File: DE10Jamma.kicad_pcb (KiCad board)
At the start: 2 copper layers, 114.6 x 83.4 mm, 104 parts, among them J1 Arduino 3-7, J10 5V TO DE10, J2 Arduino 8-SCL, J3 FAN 12V, J4 FAN 5V, J5 FAN 3V3, J6 Arduino Reset, J7 GPIO1, J8 Jamma_con, J9 CPS1 KICK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

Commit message: clean before sending to manufacture
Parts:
- added J11: 0.1" kick, Connector_PinHeader_2.54mm:PinHeader_1x10_P2.54mm_Vertical, F.Cu at (93.7, 85.5)
- moved R8 17.2 mm to (186.4, 98.0)
- moved R73 2.99 mm to (103.3, 47.9)
- moved R113 1.74 mm to (160.4, 66.8)
- moved C38 1.17 mm to (104.9, 52.7)
- moved C11 0.26 mm to (189.1, 85.7)
- moved R110 0.13 mm to (159.2, 59.2)
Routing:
- net GND: track 331.9 -> 86.3 mm, vias 81 -> 121
- net Net-(C7-Pad1): track 68.6 -> 39.2 mm
- net /P1_BUTTON5: track 81.9 -> 97.4 mm
- net /P1_BUTTON4: track 110.2 -> 125.4 mm
- net Net-(R8-Pad1): track 7.62 -> 20.4 mm
- net /JAMMA_P2_BUTTON4: track 76.5 -> 84.6 mm
- net /JAMMA_SPEAKER_L: track 85.1 -> 77.5 mm
- net +12V: track 94.5 -> 89.0 mm, vias 1 -> 2
- net /JAMMA_P2_BUTTON6: track 4.00 -> 9.02 mm
- net /JAMMA_P2_BUTTON5: track 4.00 -> 9.00 mm
- net /JAMMA_P1_BUTTON6: track 4.00 -> 8.95 mm
- net /JAMMA_P1_BUTTON5: track 4.00 -> 8.94 mm
- net /JAMMA_P1_BUTTON4: track 55.8 -> 60.5 mm
- net +5V: track 104.9 -> 109.3 mm, vias 2 -> 4
- net +5VL: track 113.1 -> 117.3 mm
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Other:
- board text added: "12V"
- board text added: "3V3"
- board text added: "5V"
- board text added: "BLUE"
- board text added: "CPS1 KICK"
- board text added: "DE10 Jamma v1.0"
- board text added: "GND"
- board text added: "GREEN"
- board text added: "L"
- board text added: "P1B4"
- board text added: "P1B5"
- board text added: "P1B6"
- board text added: "P2B4"
- board text added: "P2B5"
- board text added: "P2B6"
- board text added: "R"
- board text added: "RED"
- board text added: "VOLUME"
- board text added: "https://github.com/MisterJamma/DE10Jamma"
- board text removed: "DE10 Jamma"

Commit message: Add mono/stereo jumper. Remove out of date pdf
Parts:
- added JP1: Mono/Stereo, Connector_PinHeader_2.54mm:PinHeader_1x03_P2.54mm_Vertical, F.Cu at (186.9, 60.7)
- added R5: 10k, Capacitor_SMD:C_0805_2012Metric, B.Cu at (192.7, 67.0)
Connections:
- U1 pad 1: Net-(C5-Pad2) -> Net-(JP1-Pad1)
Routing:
- net Net-(JP1-Pad1): track 0.00 -> 10.8 mm
- net Net-(C6-Pad2): track 2.29 -> 12.1 mm
- net Net-(C5-Pad2): track 2.29 -> 7.28 mm
- net GND: vias 121 -> 120
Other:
- board text added: "JLCJLCJLCJLC"
- board text added: "MONO/STEREO"

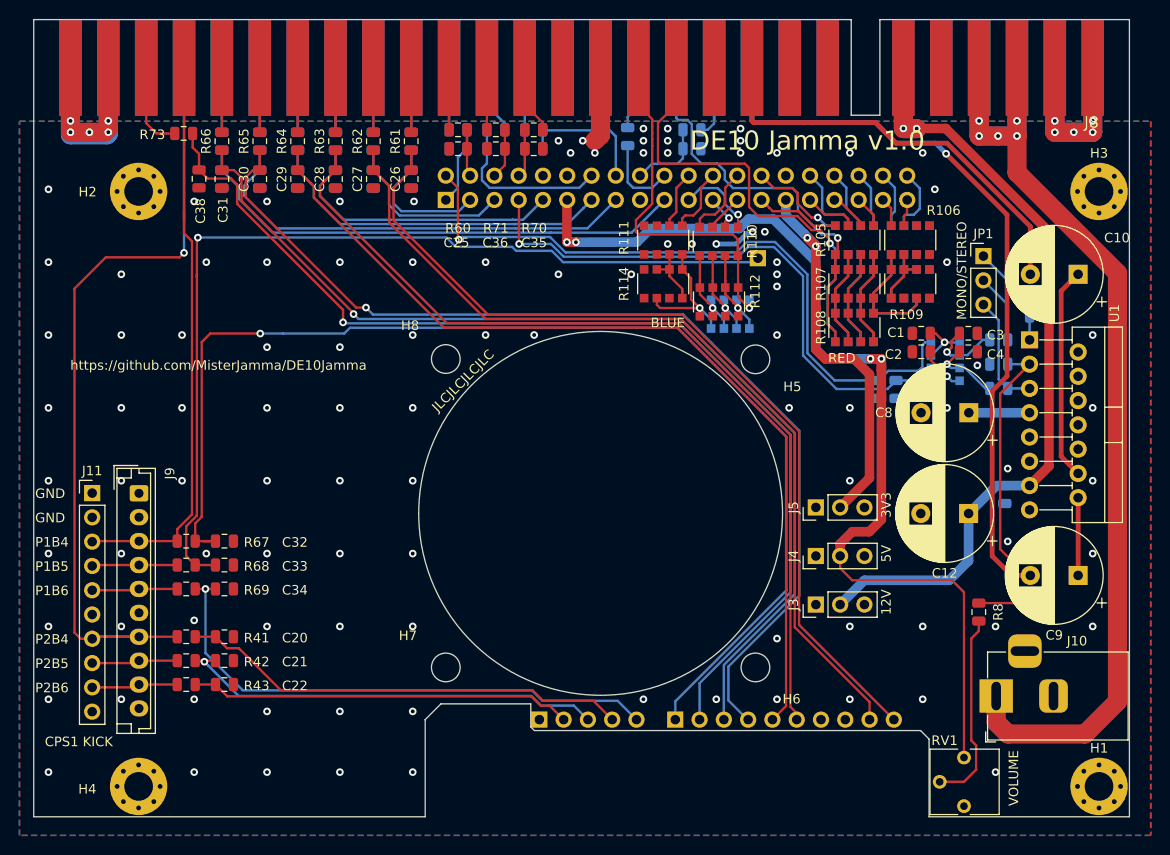
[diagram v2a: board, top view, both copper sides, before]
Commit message: Use smaller footprint for r-packs. Rework mono/stereo jumper to avoid potential DC path issues if inputs have DC offset. General routing & silk screen cleanup.
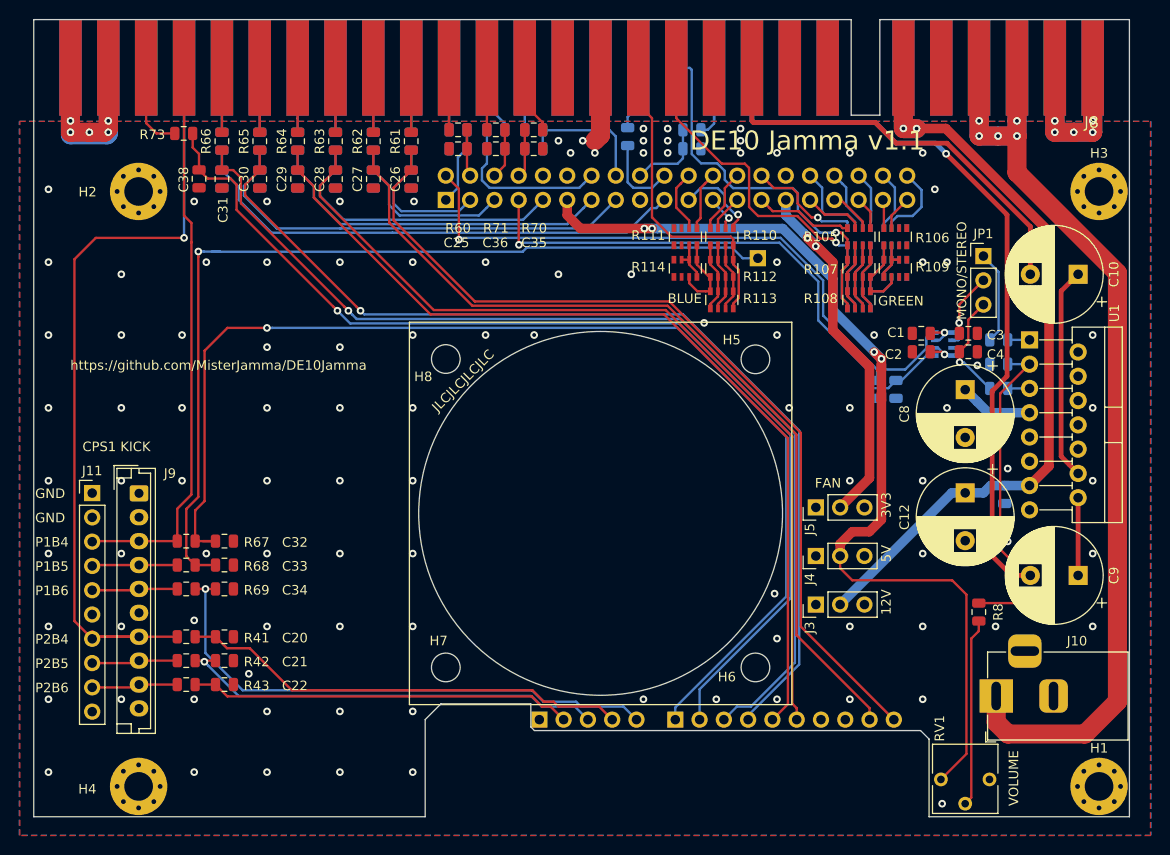
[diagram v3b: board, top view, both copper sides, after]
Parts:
- removed R5: 10k, Capacitor_SMD:C_0805_2012Metric
- R100, R101, R102, R103, R104, R105, R106, R107, R108, R109, R110, R111, R112, R114, R4: footprint Resistor_SMD:R_Array_Convex_4x1206 -> Resistor_SMD:R_Array_Convex_4x0603
- R113: footprint Resistor_SMD:R_Array_Convex_4x1206 -> Resistor_SMD:R_Array_Convex_4x0603; moved to F.Cu
- moved R112 3.52 mm to (159.6, 62.0)
- moved RV1 3.32 mm to (182.5, 115.5), turned to 270 degrees
- moved R103 2.92 mm to (173.9, 65.3)
- moved R108 2.92 mm to (173.9, 65.3)
- moved R114 2.83 mm to (155.7, 62.0)
- moved C8 2.44 mm to (185.0, 74.7), turned to 270 degrees
- moved R111 2.35 mm to (155.7, 58.7)
- moved R104 2.25 mm to (177.7, 62.0)
- moved R109 2.25 mm to (177.7, 62.0)
- moved C12 2.19 mm to (185.0, 85.5), turned to 270 degrees
- moved R4 1.85 mm to (182.7, 69.9)
- moved R113 1.73 mm to (159.6, 65.3), turned to 270 degrees
- moved R102 1.68 mm to (173.9, 62.0)
- moved R107 1.68 mm to (173.9, 62.0)
- moved R101 1.60 mm to (177.7, 58.7)
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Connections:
- C5 pad 1: Net-(C3-Pad1) -> Net-(C5-Pad1)
- H5 pad 1: (no net) -> GND
- H6 pad 1: (no net) -> GND
- H7 pad 1: (no net) -> GND
- H8 pad 1: (no net) -> GND
- J1 pad 1: Net-(J1-Pad1) -> (no net)
- J11 pad 10: Net-(J11-Pad10) -> (no net)
- J11 pad 6: Net-(J11-Pad6) -> (no net)
- J2 pad 8: Net-(J2-Pad8) -> (no net)
- J3 pad 3: Net-(J3-Pad3) -> (no net)
- J4 pad 3: Net-(J4-Pad3) -> (no net)
- J5 pad 3: Net-(J5-Pad3) -> (no net)
- J7 pad 17: Net-(J7-Pad17) -> (no net)
- J8 pad 11: Net-(J8-Pad11) -> (no net)
- J8 pad 15: Net-(J8-Pad15) -> (no net)
- J8 pad 5: Net-(J8-Pad5) -> (no net)
- J8 pad 8: Net-(J8-Pad8) -> (no net)
- J8 pad 9: Net-(J8-Pad9) -> (no net)
- J8 pad E: Net-(J8-PadE) -> (no net)
- J8 pad J: Net-(J8-PadJ) -> (no net)
- J8 pad K: Net-(J8-PadK) -> (no net)
- J8 pad R: Net-(J8-PadR) -> (no net)
- J8 pad S: Net-(J8-PadS) -> (no net)
- J8 pad d: Net-(J8-Padd) -> (no net)
- J9 pad 10: Net-(J9-Pad10) -> (no net)
- J9 pad 6: Net-(J9-Pad6) -> (no net)
- JP1 pad 1: Net-(JP1-Pad1) -> Net-(C5-Pad1)
- JP1 pad 2: Net-(C5-Pad2) -> Net-(C3-Pad1)
- JP1 pad 3: Net-(C6-Pad2) -> Net-(C4-Pad1)
- R104 pad 6: Net-(R101-Pad8) -> GND
- R104 pad 7: GND -> Net-(R101-Pad8)
- R109 pad 2: GND -> Net-(R106-Pad1)
- R109 pad 3: Net-(R106-Pad1) -> GND
- R114 pad 6: Net-(R111-Pad8) -> GND
- R114 pad 7: GND -> Net-(R111-Pad8)
- U1 pad 1: Net-(JP1-Pad1) -> Net-(C5-Pad2)
- U1 pad 2: Net-(U1-Pad2) -> (no net)
- U1 pad 4: Net-(U1-Pad4) -> (no net)
- U1 pad 6: Net-(U1-Pad6) -> (no net)
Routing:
- net Net-(JP1-Pad1): track 10.8 -> 0.00 mm
- net Net-(C5-Pad1): track 0.00 -> 9.83 mm
- net Net-(C6-Pad2): track 12.1 -> 2.29 mm
- net /JAMMA_VIDEO_R: track 45.9 -> 38.1 mm
- net Net-(R111-Pad8): track 16.0 -> 8.67 mm, vias 1 -> 0
- net Net-(C4-Pad1): track 7.42 -> 13.6 mm
- net Net-(C5-Pad2): track 7.28 -> 2.29 mm
- net /JAMMA_VIDEO_B: track 38.1 -> 33.4 mm, vias 1 -> 0
- net GND: track 86.3 -> 82.0 mm, vias 120 -> 118
- net Net-(R101-Pad8): track 12.5 -> 8.66 mm
- net Net-(R106-Pad1): track 12.5 -> 8.66 mm
- net +5V: track 109.3 -> 105.7 mm
- net Net-(R110-Pad6): track 10.6 -> 7.27 mm, vias 1 -> 0
- net Net-(R110-Pad5): track 10.6 -> 7.37 mm, vias 1 -> 0
- net Net-(R110-Pad7): track 10.6 -> 7.50 mm, vias 1 -> 0
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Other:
- board text added: "DE10 Jamma v1.1"
- board text added: "FAN"
- board text removed: "DE10 Jamma v1.0"

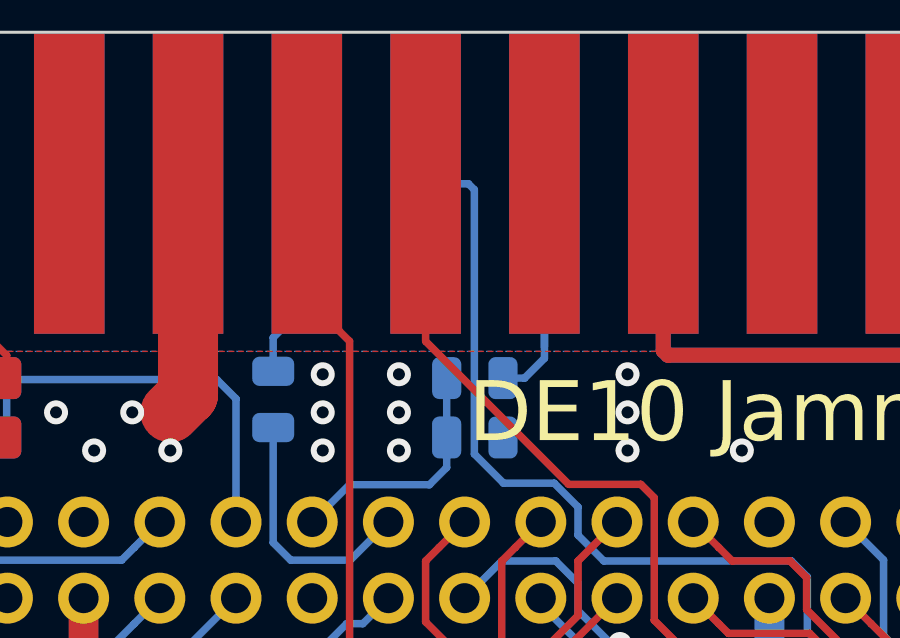
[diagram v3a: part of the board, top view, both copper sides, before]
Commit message: Route wire into JAMMA _VIDEO_G pad properly
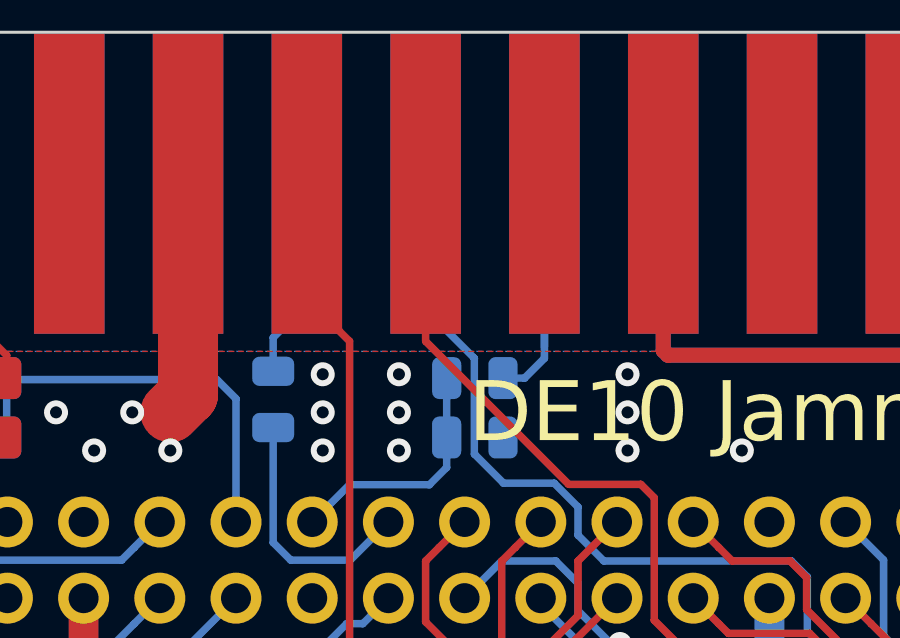
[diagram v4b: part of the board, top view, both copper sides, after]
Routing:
- net /JAMMA_VIDEO_G: track 39.8 -> 39.0 mm
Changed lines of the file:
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@@
   (segment (start 172.114999 62.219321) (end 172.69508 61.63924) (width 0.25) (layer F.Cu) (net 74))
   (segment (start 172.69508 61.63924) (end 172.69 61.63416) (width 0.25) (layer F.Cu) (net 74))
-  (segment (start 159.863 52.763002) (end 160.722998 53.623) (width 0.25) (layer B.Cu) (net 74))
+  (segment (start 172.69 59.614) (end 172.69 58.964) (width 0.25) (layer F.Cu) (net 74))
+  (segment (start 172.69 58.964) (end 172.005422 58.279422) (width 0.25) (layer F.Cu) (net 74))
+  (segment (start 172.005422 58.279422) (end 171.498896 58.279422) (width 0.25) (layer F.Cu) (net 74))
+  (via (at 171.498896 58.279422) (size 0.8) (drill 0.4) (layers F.Cu B.Cu) (net 74))
   (segment (start 170.933211 58.279422) (end 171.498896 58.279422) (width 0.25) (layer B.Cu) (net 74))
+  (segment (start 167.5084 55.9852) (end 169.802622 58.279422) (width 0.25) (layer B.Cu) (net 74))
+  (segment (start 160.722998 53.623) (end 166.975 53.623) (width 0.25) (layer B.Cu) (net 74))
+  (segment (start 156.4086 46.8666) (end 156.4086 50.05985) (width 0.25) (layer B.Cu) (net 74))
   (segment (start 166.975 53.623) (end 167.5084 54.1564) (width 0.25) (layer B.Cu) (net 74))
-  (segment (start 156.4086 41.2496) (end 156.4086 50.05985) (width 0.25) (layer B.Cu) (net 74))
+  (segment (start 154.784 41.05) (end 154.784 45.242) (width 0.25) (layer B.Cu) (net 74))
   (segment (start 157.38095 51.0322) (end 159.070202 51.0322) (width 0.25) (layer B.Cu) (net 74))
-  (segment (start 156.209 41.05) (end 156.4086 41.2496) (width 0.25) (layer B.Cu) (net 74))
+  (segment (start 154.784 45.242) (end 156.4086 46.8666) (width 0.25) (layer B.Cu) (net 74))
+  (segment (start 169.802622 58.279422) (end 170.933211 58.279422) (width 0.25) (layer B.Cu) (net 74))
+  (segment (start 167.5084 54.1564) (end 167.5084 55.9852) (width 0.25) (layer B.Cu) (net 74))
   (segment (start 159.070202 51.0322) (end 159.863 51.824998) (width 0.25) (layer B.Cu) (net 74))
   (segment (start 159.863 51.824998) (end 159.863 52.763002) (width 0.25) (layer B.Cu) (net 74))
-  (segment (start 172.69 59.614) (end 172.69 58.964) (width 0.25) (layer F.Cu) (net 74))
-  (segment (start 160.722998 53.623) (end 166.975 53.623) (width 0.25) (layer B.Cu) (net 74))
   (segment (start 156.4086 50.05985) (end 157.38095 51.0322) (width 0.25) (layer B.Cu) (net 74))
-  (segment (start 154.784 41.05) (end 156.209 41.05) (width 0.25) (layer B.Cu) (net 74))
-  (segment (start 172.69 58.964) (end 172.005422 58.279422) (width 0.25) (layer F.Cu) (net 74))
-  (segment (start 167.5084 54.1564) (end 167.5084 55.9852) (width 0.25) (layer B.Cu) (net 74))
-  (segment (start 169.802622 58.279422) (end 170.933211 58.279422) (width 0.25) (layer B.Cu) (net 74))
-  (segment (start 172.005422 58.279422) (end 171.498896 58.279422) (width 0.25) (layer F.Cu) (net 74))
-  (via (at 171.498896 58.279422) (size 0.8) (drill 0.4) (layers F.Cu B.Cu) (net 74))
-  (segment (start 167.5084 55.9852) (end 169.802622 58.279422) (width 0.25) (layer B.Cu) (net 74))
+  (segment (start 159.863 52.763002) (end 160.722998 53.623) (width 0.25) (layer B.Cu) (net 74))
   (segment (start 150.846 41.072) (end 150.824 41.05) (width 0.25) (layer F.Cu) (net 75))
   (segment (start 160.752 59.614) (end 160.752 61.116) (width 0.25) (layer F.Cu) (net 75))
